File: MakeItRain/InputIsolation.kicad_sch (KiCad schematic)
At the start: 2 parts, among them IC2 LTV-846S, IC3 SN7404DR

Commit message: wip
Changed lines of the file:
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@@
 (kicad_sch (version 20211123) (generator eeschema)
   (paper "A4")
+  (hierarchical_label "4in" (shape input) (at 99.06 87.63 180)
+    (effects (font (size 1.27 1.27)) (justify right))
+  )
+  (hierarchical_label "2out" (shape input) (at 101.6 115.57 180)
+    (effects (font (size 1.27 1.27)) (justify right))
+  )
+  (hierarchical_label "3out" (shape input) (at 101.6 118.11 180)
+    (effects (font (size 1.27 1.27)) (justify right))
+  )
+  (hierarchical_label "3in" (shape input) (at 99.06 85.09 180)
+    (effects (font (size 1.27 1.27)) (justify right))
+  )
+  (hierarchical_label "2in" (shape input) (at 99.06 82.55 180)
+    (effects (font (size 1.27 1.27)) (justify right))
+  )
+  (hierarchical_label "1out" (shape input) (at 101.6 113.03 180)
+    (effects (font (size 1.27 1.27)) (justify right))
+  )
+  (hierarchical_label "1in" (shape input) (at 99.06 80.01 180)
+    (effects (font (size 1.27 1.27)) (justify right))
+  )
+  (hierarchical_label "4out" (shape input) (at 101.6 120.65 180)
+    (effects (font (size 1.27 1.27)) (justify right))
+  )
   (symbol (lib_id "Samac_Sys:LTV-846S") (at 133.35 82.55 0) (unit 1)
     (in_bom yes) (on_board yes) (fields_autoplaced)

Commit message: wip for input fix.
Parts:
- removed IC3: SN7404DR, SOIC127P600X175-14N, symbol Samac_Sys:SN7404DR
- added R24, R25, R26, R27, R28, R29, R30, R31: 10k, Resistor_THT:R_Axial_DIN0207_L6.3mm_D2.5mm_P2.54mm_Vertical, symbol Device:R
- renumbered IC2 to IC4
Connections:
- net 1in: now also IC4.2 (K_1)
- net 1out: now also IC4.16 (C_4), R28.2
- net 2in: now also IC4.4 (K_2)
- net 2out: now also IC4.14 (C_3), R29.2
- net 3in: now also IC4.6 (K_3)
- net 3out: now also IC4.12 (C_2), R30.2
- net 4in: now also IC4.8 (K_4)
- net 4out: now also IC4.10 (C_1), R31.2
- net at IC4.1 (A_1): now also R27.2
- net GND: now reaches IC4.11 (E_2)
- net GND: now also IC4.13 (E_3), IC4.15 (E_4), IC4.9 (E_1)
- net at IC4.3 (A_2): now also R26.2
- net at IC4.5 (A_3): now also R25.2
- net at IC4.7 (A_4): now also R24.2
- new net +3V3: R24.1, R25.1, R26.1, R27.1, R28.1, R29.1, R30.1, R31.1
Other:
- moved on the sheet: IC4

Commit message: wip for layout
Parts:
- renumbered R24 to R26, R25 to R27, R26 to R28, R27 to R29, R28 to R30, R29 to R31, R30 to R32, R31 to R33
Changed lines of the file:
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@@
   (symbol (lib_id "Device:R") (at 78.74 44.45 0) (unit 1)
     (in_bom yes) (on_board yes)
-    (property "Reference" "R24" (id 0) (at 80.518 43.2816 0)
+    (property "Reference" "R26" (id 0) (at 80.518 43.2816 0)
       (effects (font (size 1.27 1.27)) (justify left))
     )
@@
   (symbol (lib_id "Device:R") (at 177.8 45.72 0) (unit 1)
     (in_bom yes) (on_board yes)
-    (property "Reference" "R30" (id 0) (at 179.578 44.5516 0)
+    (property "Reference" "R32" (id 0) (at 179.578 44.5516 0)
       (effects (font (size 1.27 1.27)) (justify left))
     )
@@
   (symbol (lib_id "Device:R") (at 170.18 45.72 0) (unit 1)
     (in_bom yes) (on_board yes)
-    (property "Reference" "R29" (id 0) (at 171.958 44.5516 0)
+    (property "Reference" "R31" (id 0) (at 171.958 44.5516 0)
       (effects (font (size 1.27 1.27)) (justify left))
     )
@@
   (symbol (lib_id "power:+3.3V") (at 184.15 35.56 0) (unit 1)
     (in_bom yes) (on_board yes)
-    (property "Reference" "#PWR052" (id 0) (at 184.15 39.37 0)
+    (property "Reference" "#PWR055" (id 0) (at 184.15 39.37 0)
       (effects (font (size 1.27 1.27)) hide)
     )
@@
   (symbol (lib_id "power:+3.3V") (at 170.18 35.56 0) (unit 1)
     (in_bom yes) (on_board yes)
-    (property "Reference" "#PWR050" (id 0) (at 170.18 39.37 0)
+    (property "Reference" "#PWR053" (id 0) (at 170.18 39.37 0)
       (effects (font (size 1.27 1.27)) hide)
     )
@@
   (symbol (lib_id "power:GND") (at 154.94 78.74 0) (unit 1)
     (in_bom yes) (on_board yes)
-    (property "Reference" "#PWR048" (id 0) (at 154.94 85.09 0)
+    (property "Reference" "#PWR051" (id 0) (at 154.94 85.09 0)
       (effects (font (size 1.27 1.27)) hide)
     )
@@
   (symbol (lib_id "Device:R") (at 85.09 44.45 0) (unit 1)
     (in_bom yes) (on_board yes)
-    (property "Reference" "R25" (id 0) (at 86.868 43.2816 0)
+    (property "Reference" "R27" (id 0) (at 86.868 43.2816 0)
       (effects (font (size 1.27 1.27)) (justify left))
     )
@@
   (symbol (lib_id "power:+3.3V") (at 177.8 35.56 0) (unit 1)
     (in_bom yes) (on_board yes)
-    (property "Reference" "#PWR051" (id 0) (at 177.8 39.37 0)
+    (property "Reference" "#PWR054" (id 0) (at 177.8 39.37 0)
       (effects (font (size 1.27 1.27)) hide)
     )
@@
   (symbol (lib_id "Device:R") (at 92.71 44.45 0) (unit 1)
     (in_bom yes) (on_board yes)
-    (property "Reference" "R26" (id 0) (at 94.488 43.2816 0)
+    (property "Reference" "R28" (id 0) (at 94.488 43.2816 0)
       (effects (font (size 1.27 1.27)) (justify left))
     )
@@
   (symbol (lib_id "Device:R") (at 99.06 44.45 0) (unit 1)
     (in_bom yes) (on_board yes)
-    (property "Reference" "R27" (id 0) (at 100.838 43.2816 0)
+    (property "Reference" "R29" (id 0) (at 100.838 43.2816 0)
       (effects (font (size 1.27 1.27)) (justify left))
     )
@@
   (symbol (lib_id "power:+3.3V") (at 99.06 34.29 0) (unit 1)
     (in_bom yes) (on_board yes)
-    (property "Reference" "#PWR047" (id 0) (at 99.06 38.1 0)
+    (property "Reference" "#PWR050" (id 0) (at 99.06 38.1 0)
       (effects (font (size 1.27 1.27)) hide)
     )
@@
   (symbol (lib_id "power:+3.3V") (at 92.71 34.29 0) (unit 1)
     (in_bom yes) (on_board yes)
-    (property "Reference" "#PWR046" (id 0) (at 92.71 38.1 0)
+    (property "Reference" "#PWR049" (id 0) (at 92.71 38.1 0)
       (effects (font (size 1.27 1.27)) hide)
     )
@@
   (symbol (lib_id "power:+3.3V") (at 163.83 35.56 0) (unit 1)
     (in_bom yes) (on_board yes)
-    (property "Reference" "#PWR049" (id 0) (at 163.83 39.37 0)
+    (property "Reference" "#PWR052" (id 0) (at 163.83 39.37 0)
       (effects (font (size 1.27 1.27)) hide)
     )
@@
   (symbol (lib_id "power:+3.3V") (at 78.74 34.29 0) (unit 1)
     (in_bom yes) (on_board yes)
-    (property "Reference" "#PWR044" (id 0) (at 78.74 38.1 0)
+    (property "Reference" "#PWR047" (id 0) (at 78.74 38.1 0)
       (effects (font (size 1.27 1.27)) hide)
     )
@@
   (symbol (lib_id "Device:R") (at 184.15 45.72 0) (unit 1)
     (in_bom yes) (on_board yes)
-    (property "Reference" "R31" (id 0) (at 185.928 44.5516 0)
+    (property "Reference" "R33" (id 0) (at 185.928 44.5516 0)
       (effects (font (size 1.27 1.27)) (justify left))
     )
@@
   (symbol (lib_id "power:+3.3V") (at 85.09 34.29 0) (unit 1)
     (in_bom yes) (on_board yes)
-    (property "Reference" "#PWR045" (id 0) (at 85.09 38.1 0)
+    (property "Reference" "#PWR048" (id 0) (at 85.09 38.1 0)
       (effects (font (size 1.27 1.27)) hide)
     )
@@
   (symbol (lib_id "Device:R") (at 163.83 45.72 0) (unit 1)
     (in_bom yes) (on_board yes)
-    (property "Reference" "R28" (id 0) (at 165.608 44.5516 0)
-      (effects (font (size 1.27 1.27)) (justify left))
-    )
+    (property "Reference" "R30" (id 0) (at 165.608 44.5516 0)
+      (effects (font (size 1.27 1.27)) (justify left))
+    )

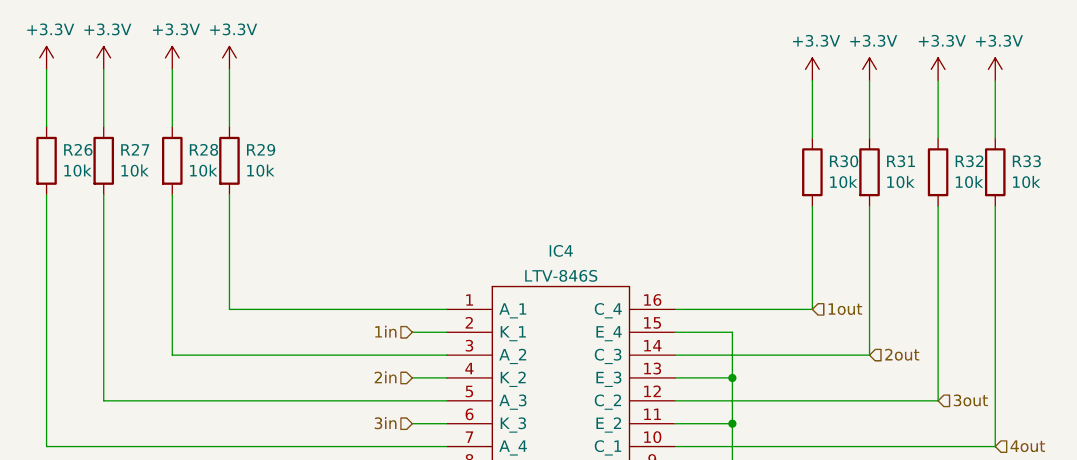
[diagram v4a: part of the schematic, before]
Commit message: updated values for the InputIsolation circuits. updated the PCB values and BOM. Updating the Hardware Validation program.
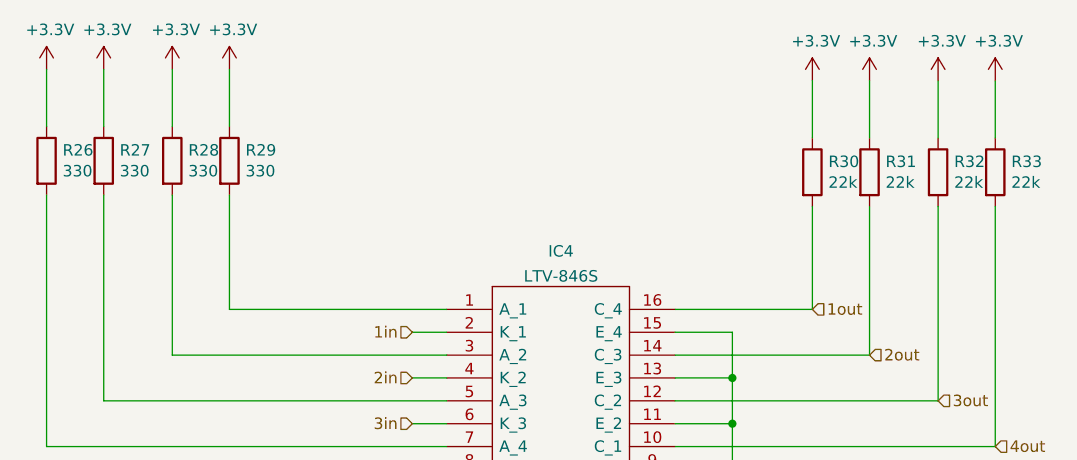
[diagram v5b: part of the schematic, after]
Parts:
- R26, R27, R28, R29: value 10k -> 330
- R30, R31, R32, R33: value 10k -> 22k
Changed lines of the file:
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@@
       (effects (font (size 1.27 1.27)) (justify left))
     )
-    (property "Value" "10k" (id 1) (at 80.518 45.593 0)
+    (property "Value" "330" (id 1) (at 80.518 45.593 0)
       (effects (font (size 1.27 1.27)) (justify left))
     )
@@
       (effects (font (size 1.27 1.27)) (justify left))
     )
-    (property "Value" "10k" (id 1) (at 179.578 46.863 0)
+    (property "Value" "22k" (id 1) (at 179.578 46.863 0)
       (effects (font (size 1.27 1.27)) (justify left))
     )
@@
       (effects (font (size 1.27 1.27)) (justify left))
     )
-    (property "Value" "10k" (id 1) (at 171.958 46.863 0)
+    (property "Value" "22k" (id 1) (at 171.958 46.863 0)
       (effects (font (size 1.27 1.27)) (justify left))
     )
@@
       (effects (font (size 1.27 1.27)) (justify left))
     )
-    (property "Value" "10k" (id 1) (at 86.868 45.593 0)
+    (property "Value" "330" (id 1) (at 86.868 45.593 0)
       (effects (font (size 1.27 1.27)) (justify left))
     )
@@
       (effects (font (size 1.27 1.27)) (justify left))
     )
-    (property "Value" "10k" (id 1) (at 94.488 45.593 0)
+    (property "Value" "330" (id 1) (at 94.488 45.593 0)
       (effects (font (size 1.27 1.27)) (justify left))
     )
@@
       (effects (font (size 1.27 1.27)) (justify left))
     )
-    (property "Value" "10k" (id 1) (at 100.838 45.593 0)
+    (property "Value" "330" (id 1) (at 100.838 45.593 0)
       (effects (font (size 1.27 1.27)) (justify left))
     )
@@
       (effects (font (size 1.27 1.27)) (justify left))
     )
-    (property "Value" "10k" (id 1) (at 185.928 46.863 0)
+    (property "Value" "22k" (id 1) (at 185.928 46.863 0)
       (effects (font (size 1.27 1.27)) (justify left))
     )
@@
       (effects (font (size 1.27 1.27)) (justify left))
     )
-    (property "Value" "10k" (id 1) (at 165.608 46.863 0)
-      (effects (font (size 1.27 1.27)) (justify left))
-    )
+    (property "Value" "22k" (id 1) (at 165.608 46.863 0)
+      (effects (font (size 1.27 1.27)) (justify left))
+    )

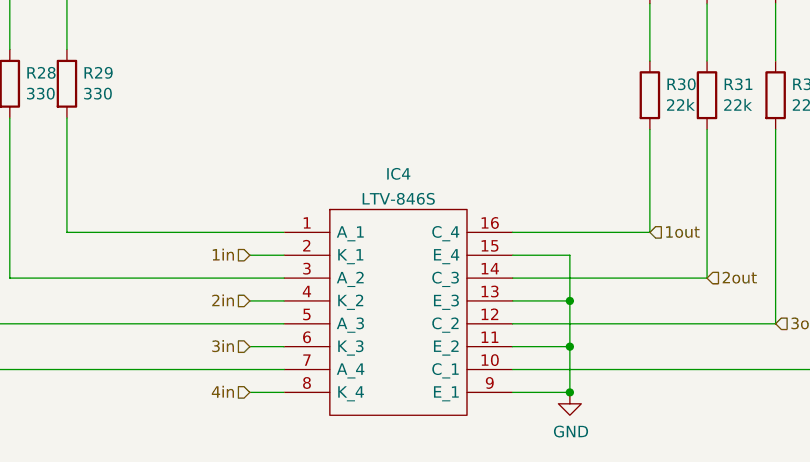
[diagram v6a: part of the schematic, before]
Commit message: MakeItRain * Main Board Fixed Routing. * replaced Opamp with the part that i can get as the old one is EOL * generated all the fab files i need. * updated the daughter plug witht eh i2c ttl flip * fixed I2C issues * DRC'ed the board
MakeItRain - DaughterBoard - Zone Expansion
* updated the daughter plug witht eh i2c ttl flip
* fixed some of the routings
* generated new fab files
* DRC'ed the board
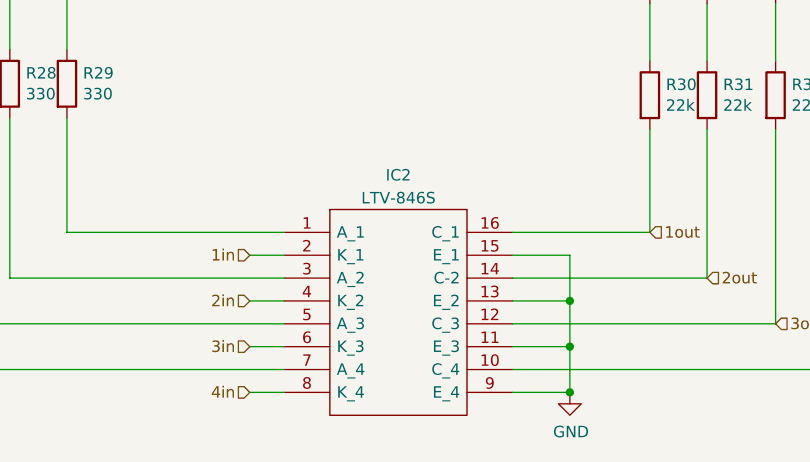
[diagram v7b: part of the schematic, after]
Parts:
- removed IC4: LTV-846S, SOP254P1016X460-16N, symbol Samac_Sys:LTV-846S
- added IC2: LTV-846S, LTV846S, symbol SamacSys_Parts:LTV-846S
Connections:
- net 1in: now also IC2.2 (K_1)
- net 1out: now also IC2.16 (C_1)
- net 2in: now also IC2.4 (K_2)
- net 2out: now also IC2.14 (C-2)
- net 3in: now also IC2.6 (K_3)
- net 3out: now also IC2.12 (C_3)
- net 4in: now also IC2.8 (K_4)
- net 4out: now also IC2.10 (C_4)
- net GND: now also IC2.11 (E_3), IC2.13 (E_2), IC2.15 (E_1), IC2.9 (E_4)
- net at R26.2: now also IC2.7 (A_4)
- net at R27.2: now also IC2.5 (A_3)
- net at R28.2: now also IC2.3 (A_2)
- net at R29.2: now also IC2.1 (A_1)

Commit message: imput redesign
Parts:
- added C2 (x4): 220nF, Capacitor_THT:C_Disc_D5.1mm_W3.2mm_P5.00mm, symbol Device:C
- added Q14, Q15, Q16, Q17: BS250, Package_TO_SOT_THT:TO-92_Inline, symbol Transistor_FET:BS250
- added R39, R41: 330, Resistor_THT:R_Axial_DIN0207_L6.3mm_D2.5mm_P2.54mm_Vertical, symbol Device:R
- added R40, R42: 1K, Resistor_THT:R_Axial_DIN0207_L6.3mm_D2.5mm_P2.54mm_Vertical, symbol Device:R
- R27, R29: value 330 -> 1K
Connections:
- net +3V3: now also IC2.10 (C_4), IC2.12 (C_3), IC2.14 (C-2), IC2.16 (C_1); no longer R26.1, R27.1, R28.1, R29.1, R30.1, R31.1, R32.1, R33.1
- net 1in: now also C2.1, Q14.3 (S); no longer IC2.2 (K_1)
- net 1out: now also IC2.15 (E_1), R32.1; no longer IC2.16 (C_1), R30.2
- net 2in: now also C2.1, Q15.3 (S); no longer IC2.4 (K_2)
- net 2out: now also IC2.13 (E_2), R33.1; no longer IC2.14 (C-2), R31.2
- net 3in: now also C2.1, Q16.3 (S); no longer IC2.6 (K_3)
- net 3out: now also IC2.11 (E_3), R31.1; no longer IC2.12 (C_3), R32.2
- net 4in: now also C2.1, Q17.3 (S); no longer IC2.8 (K_4)
- net 4out: now also IC2.9 (E_4), R30.1; no longer IC2.10 (C_4), R33.2
- net GND: now also IC2.2 (K_1), IC2.4 (K_2), IC2.6 (K_3), IC2.8 (K_4), R26.2, R28.2, R30.2, R31.2, R32.2, R33.2, C2.2, C2.2, C2.2, C2.2, R39.2, R41.2; no longer IC2.11 (E_3), IC2.13 (E_2), IC2.15 (E_1), IC2.9 (E_4)
- net at IC2.7 (A_4): now also R42.2; no longer R26.2
- net at R27.2: now also IC2.3 (A_2); no longer IC2.5 (A_3)
- net at IC2.1 (A_1): now also R40.2; no longer R29.2
- new net: Q14.1 (D), R40.1
- new net: Q14.2 (G), R39.1
- new net: Q15.1 (D), R27.1
- new net: Q16.1 (D), R29.1
- new net: Q16.2 (G), R28.1
- new net: Q17.2 (G), R41.1
- new net: Q17.1 (D), R42.1
- new net: Q15.2 (G), R26.1
- new net: IC2.5 (A_3), R29.2
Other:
- moved on the sheet: R30, R31, R32, R33
